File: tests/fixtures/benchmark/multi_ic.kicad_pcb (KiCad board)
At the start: 4 copper layers, 100 x 80 mm, 52 parts, among them J1 USB_C, J2 RJ45, J3 SWD, J4 CAN, J5 UART1, SW1 RESET, T1 749010012A, U1 STM32F407VGT6, U2 LAN8720A, U3 W25Q32JVSS, U4 AMS1117-3.3, U5 AP2112K-1.8, U6 SN65HVD230, U7 USBLC6-2SC6, Y1 8MHz, Y2 25MHz

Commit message: fix(kicad): a coordinate that will not parse is an error, not a zero
multi_ic.kicad_pcb carries `(at 105, 80)` on line 884 and `(at 140, 55)`
on line 908 - one comma each, the only two of their kind in five
fixtures. The importer read every coordinate with `unwrap_or(0.0)`, so a
ferrite bead and an Ethernet transformer imported 50mm to the left of the
board, in silence. That is exactly the ten off-board pads the fixture
test added last commit had been reporting, and every routing number ever
measured on multi_ic was measured with those parts out there.

The parser refuses what it cannot read now:

  Error: × Failed to parse KiCad PCB file: multi_ic.kicad_pcb
    ╰─▶ Invalid data: footprint position x is not a number: String("105,").
        A coordinate must be a plain decimal, so `(at 105, 80)` is one
        comma away from `(at 105 80)`.

A board file is written by machines and edited by people. Putting a part
50mm from where the file says is worse than refusing to read the file.

The fixture test then caught its own list going stale, which is the shape
it was given for exactly this:

  multi_ic.kicad_pcb: 0 pads outside the board outline, 10 known

stm32_breakout (8) and shift_driver (6) still match theirs.

Re-measured with the two parts back on the board:

  before  1003 routes, 270 before, 317 after, 247 introduced, 166 shorts
  after    978 routes, 281 before, 318 after, 247 introduced, 177 shorts

Its band is 63 violations wide across prices 0.22..0.28, against the 30
measured while a ferrite bead and a transformer were off the board and
out of the way. Ratchet 381 / 210, and benchmark_all_fixtures_drc passes.

  cargo fmt --check                                       clean
  cargo clippy --workspace --all-targets -- -D warnings   clean
  cargo test --workspace --exclude cypcb-desktop          no failures
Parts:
- moved T1 140.0 mm to (140.0, 55.0)
- moved FB1 105.0 mm to (105.0, 80.0)
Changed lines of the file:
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@@
   (footprint "Inductor_SMD:L_0402_1005Metric"
     (layer "F.Cu")
-    (at 105, 80)
+    (at 105 80)
     (property "Reference" "FB1")
     (property "Value" "600R@100MHz")
@@
   (footprint "Transformer_SMD:Transformer_Ethernet_Wuerth_749010012A"
     (layer "F.Cu")
-    (at 140, 55)
+    (at 140 55)
     (property "Reference" "T1")
     (property "Value" "749010012A")

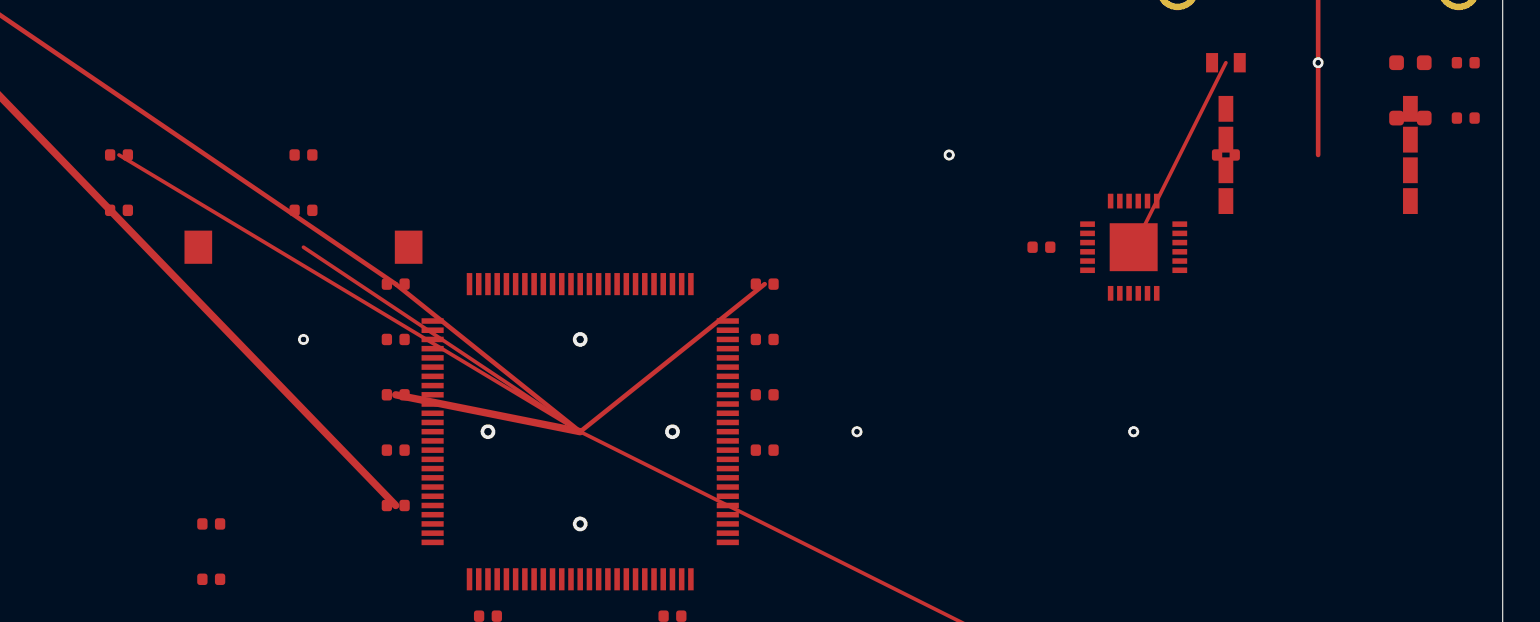
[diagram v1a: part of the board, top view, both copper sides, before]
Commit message: fix(benchmark): multi_ic asked for twelve pairs of parts in the same place
Nine of them were decoupling capacitors ringing U1 at a uniform 0.14mm where
0.25mm is required - one ring placed slightly too tight, fixed by moving both
columns 0.5mm outward. The other three were an HC49 crystal lying across its
neighbours and two parts against the Ethernet transformer.

The crystal took three attempts, because I was guessing at its size. Moved to
two apparently empty spots it collided with three more parts each time.
Measuring the footprint - pads at plus and minus 5.7mm, so 13.4mm wide with
its courtyard - placed it correctly first time after that. Read the part
before moving it.

Measured on the unrouted board before and after, so what the moves cost is
visible rather than assumed:

                        before   after
  courtyard-clearance   12       0
  solder-mask-bridge    28       20
  clearance             39       38
  edge-clearance        1        1
  unconnected-pin       2        2
  unrouted-pin          202      202
  copper touching       32       32

Nothing was introduced. Routed:

  multi_ic: 945 routes, 291 violations against 367, 187 shorts against 210

against 978 routes and 304 / 177 before. A placement repair is not an
optimisation - the shorts rose by ten - and the board is buildable now where
it was not.

The violations ratchet tightens 367 -> 354, the measured value plus the band
of 63. The shorts ratchet stays at 210 rather than the 220 that
measured-plus-band would give: 187 is comfortably under it, and raising a
ratchet to match a formula loosens it for no reason.

KNOWN_OVERLAPS is empty. Every fixture is now a board whose parts fit beside
each other, so a new entry in that list is a new defect rather than an
inheritance. The margin table in docs/routing.md is dated with the moved
numbers.

Workspace: 107 suites ok, 0 failed. Gate:
  [1/8] fmt OK [2/8] clippy OK [3/8] test OK [4/8] eslint OK [5/8] vitest OK
  [6/8] playwright OK [7/8] benc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
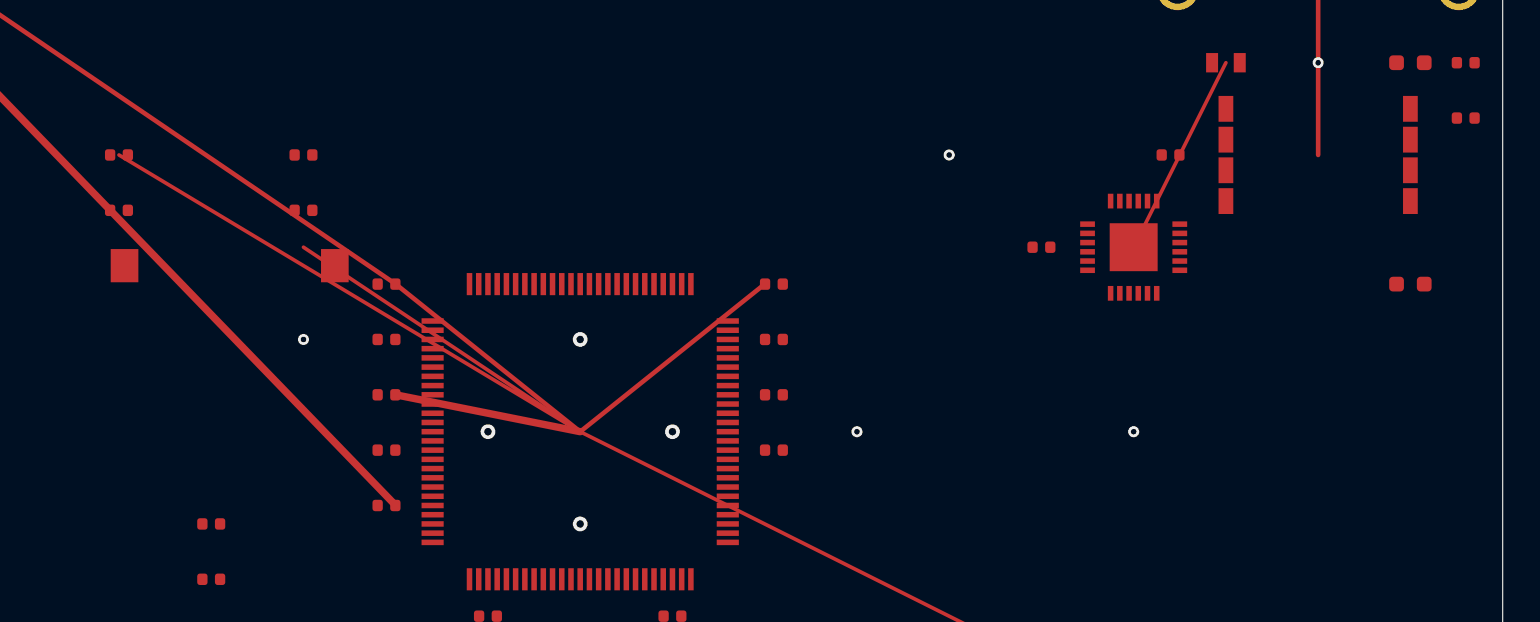
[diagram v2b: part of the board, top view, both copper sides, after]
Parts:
- moved D5 9.00 mm to (145.0, 62.0)
- moved Y1 4.12 mm to (81.0, 61.0)
- moved C12 3.00 mm to (132.0, 55.0)
- moved C1 0.50 mm to (89.5, 62.0)
- moved C2 0.50 mm to (89.5, 65.0)
- moved C3 0.50 mm to (89.5, 68.0)
- moved C4 0.50 mm to (89.5, 71.0)
- moved C5 0.50 mm to (89.5, 74.0)
- moved C6 0.50 mm to (110.5, 62.0)
- moved C7 0.50 mm to (110.5, 65.0)
- moved C8 0.50 mm to (110.5, 68.0)
- moved C9 0.50 mm to (110.5, 71.0)
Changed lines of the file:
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@@
   (footprint "Crystal:Crystal_SMD_HC49-SD"
     (layer "F.Cu")
-    (at 85 60)
+    (at 81 61)
     (property "Reference" "Y1")
     (property "Value" "8MHz")
@@
   (footprint "Capacitor_SMD:C_0402_1005Metric"
     (layer "F.Cu")
-    (at 90 62)
+    (at 89.5 62)
     (property "Reference" "C1")
     (property "Value" "100nF")
@@
   (footprint "Capacitor_SMD:C_0402_1005Metric"
     (layer "F.Cu")
-    (at 90 65)
+    (at 89.5 65)
     (property "Reference" "C2")
     (property "Value" "100nF")
@@
   (footprint "Capacitor_SMD:C_0402_1005Metric"
     (layer "F.Cu")
-    (at 90 68)
+    (at 89.5 68)
     (property "Reference" "C3")
     (property "Value" "100nF")
@@
   (footprint "Capacitor_SMD:C_0402_1005Metric"
     (layer "F.Cu")
-    (at 90 71)
+    (at 89.5 71)
     (property "Reference" "C4")
     (property "Value" "100nF")
@@
   (footprint "Capacitor_SMD:C_0402_1005Metric"
     (layer "F.Cu")
-    (at 90 74)
+    (at 89.5 74)
     (property "Reference" "C5")
     (property "Value" "100nF")
@@
   (footprint "Capacitor_SMD:C_0402_1005Metric"
     (layer "F.Cu")
-    (at 110 62)
+    (at 110.5 62)
     (property "Reference" "C6")
     (property "Value" "100nF")
@@
   (footprint "Capacitor_SMD:C_0402_1005Metric"
     (layer "F.Cu")
-    (at 110 65)
+    (at 110.5 65)
     (property "Reference" "C7")
     (property "Value" "100nF")
@@
   (footprint "Capacitor_SMD:C_0402_1005Metric"
     (layer "F.Cu")
-    (at 110 68)
+    (at 110.5 68)
     (property "Reference" "C8")
     (property "Value" "100nF")
@@
   (footprint "Capacitor_SMD:C_0402_1005Metric"
     (layer "F.Cu")
-    (at 110 71)
+    (at 110.5 71)
     (property "Reference" "C9")
     (property "Value" "100nF")
@@
   (footprint "Capacitor_SMD:C_0402_1005Metric"
     (layer "F.Cu")
-    (at 135 55)
+    (at 132 55)
     (property "Reference" "C12")
     (property "Value" "100nF")
@@
   (footprint "LED_SMD:LED_0603_1608Metric"
     (layer "F.Cu")
-    (at 145 53)
+    (at 145 62)
     (property "Reference" "D5")
     (property "Value" "Yellow")

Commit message: fix(benchmark): the copper the fixtures shipped was lines between part centres
multi_ic reported 32 pieces of copper touching copper at 0.00mm before
anything was routed. Reading the segments settled what they were:

  (segment (start 65 45) (end 90 62) ...)
  (segment (start 90 62) (end 100 70) ...)
  (segment (start 100 70) (end 110 62) ...)

65,45 is U4's origin, 90,62 is C1's, 100,70 is U1's. These are straight lines
drawn between part centres, so they cross every package on the way and short
against the pads they pass. All three fixtures that carried copper carried the
same decoration, shorting 1, 13 and 32 times respectively.

Removed: 3 segments and 2 vias from led_blink, 8 and 4 from stm32_breakout, 15
and 10 from multi_ic. All three now ship zero shorts.

led_blink keeps copper and it is real copper: one trace from R1 pad 2 at
(120.48, 65) to D1 pad 1 at (124.25, 65), both on LED_ANODE, adjacent parts,
nothing in between. The import path still has a fixture to prove itself on
rather than losing the coverage along with the decoration.

Every ratchet is unchanged, which is the proof this fed no measurement:

  led_blink: 21 routes, 2 violations against 2, 0 shorts against 0
  stm32_breakout: 908 routes, 239 against 239, 136 shorts against 136
  multi_ic: 945 routes, 291 against 354, 187 shorts against 210
  shift_driver: 700 routes, 81 against 93, 33 shorts against 40
  qfp_fanout: 1478 routes, 309 against 376, 147 shorts against 260
  plane_board: 181 routes, 28 against 37, 13 shorts against 18

The benchmark routes from scratch and never read it. What did read it was
cypcb check, the viewer, and the CLI's board loader - everything a person
actually points at a board.

Three test files leaned on it and were repointed rather than deleted. The
parse expectations say 1 segment and 0 vias for led_blink and no copper for
the other two, and the origin test - which exists to catch copper imported
without subtracting the board corner - measures against the new trace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
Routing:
- net VCC_3V3: track 55.8 -> 0.00 mm, vias 3 -> 0
- net USB_DP: track 49.2 -> 0.00 mm
- net GND: track 46.2 -> 0.00 mm, vias 4 -> 0
- net FLASH_CS: track 33.5 -> 0.00 mm
- net OSC_IN: track 18.0 -> 0.00 mm, vias 1 -> 0
- net ETH_TX_P: track 15.0 -> 0.00 mm, vias 1 -> 0
- net ETH_REFCLK: track 11.2 -> 0.00 mm, vias 1 -> 0
- net CAN_TX: track 11.2 -> 0.00 mm
- net LED3_K: track 3.00 -> 0.00 mm
- net LED2_K: track 3.00 -> 0.00 mm
- net LED1_K: track 3.00 -> 0.00 mm
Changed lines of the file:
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@@
   )
   ; -- Reference routing --
-  (segment (start 65 45) (end 90 62) (width 0.25) (layer "F.Cu") (net 1))
-  (segment (start 90 62) (end 100 70) (width 0.25) (layer "F.Cu") (net 1))
-  (segment (start 100 70) (end 110 62) (width 0.25) (layer "F.Cu") (net 1))
-  (segment (start 65 48.15) (end 90 74) (width 0.4) (layer "F.Cu") (net 2))
-  (segment (start 90 68) (end 100 70) (width 0.4) (layer "F.Cu") (net 2))
-  (segment (start 130 60) (end 135 50) (width 0.2) (layer "F.Cu") (net 69))
-  (segment (start 130 85) (end 100 70) (width 0.2) (layer "F.Cu") (net 57))
-  (segment (start 140 40) (end 140 55) (width 0.25) (layer "F.Cu") (net 70))
-  (segment (start 65 85) (end 75 90) (width 0.2) (layer "F.Cu") (net 93))
-  (segment (start 85 60) (end 100 70) (width 0.2) (layer "F.Cu") (net 91))
-  (segment (start 140 95) (end 143 95) (width 0.2) (layer "F.Cu") (net 88))
-  (segment (start 140 98) (end 143 98) (width 0.2) (layer "F.Cu") (net 89))
-  (segment (start 140 101) (end 143 101) (width 0.2) (layer "F.Cu") (net 90))
-  (segment (start 55 90) (end 75 90) (width 0.3) (layer "F.Cu") (net 5))
-  (segment (start 75 55) (end 100 70) (width 0.2) (layer "F.Cu") (net 5))
-  (via (at 95 70) (size 0.8) (drill 0.4) (layers "F.Cu" "B.Cu") (net 2))
-  (via (at 105 70) (size 0.8) (drill 0.4) (layers "F.Cu" "B.Cu") (net 2))
-  (via (at 100 65) (size 0.8) (drill 0.4) (layers "F.Cu" "B.Cu") (net 1))
-  (via (at 100 75) (size 0.8) (drill 0.4) (layers "F.Cu" "B.Cu") (net 1))
-  (via (at 115 70) (size 0.6) (drill 0.3) (layers "F.Cu" "B.Cu") (net 2))
-  (via (at 130 70) (size 0.6) (drill 0.3) (layers "F.Cu" "B.Cu") (net 1))
-  (via (at 120 55) (size 0.6) (drill 0.3) (layers "F.Cu" "B.Cu") (net 69))
-  (via (at 140 50) (size 0.6) (drill 0.3) (layers "F.Cu" "B.Cu") (net 70))
-  (via (at 80 90) (size 0.6) (drill 0.3) (layers "F.Cu" "B.Cu") (net 2))
-  (via (at 85 65) (size 0.6) (drill 0.3) (layers "F.Cu" "B.Cu") (net 91))
 )
